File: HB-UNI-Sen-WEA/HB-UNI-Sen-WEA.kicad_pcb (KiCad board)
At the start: 2 copper layers, 66 x 55.9 mm, 21 parts, among them J1 RAIN, J10 BATT, J2 PROG, J3 WIND_DIR, J4 I2C_1, J5 LIGHTNING, J6 ANEM, J7 RAIN_Q, J8 I2C_2, J9 I2C_3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

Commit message: add mounting holes
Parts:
- added REF**: MountingHole_2.2mm_M2_Pad_Via, MountingHole:MountingHole_2.2mm_M2_Pad_Via, F.Cu at (166.4, 105.4)
- added REF**: MountingHole_2.2mm_M2_Pad_Via, MountingHole:MountingHole_2.2mm_M2_Pad_Via, F.Cu at (182.9, 68.6)
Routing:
- net GND: vias 259 -> 0
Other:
- outline, holes or cut-outs redrawn

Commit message: fix typos
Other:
- board text added: "HB-UNI-SEN-WEA-PCB"
- board text removed: "HB-UNI-SENS-WEA-PCB"
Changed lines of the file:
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@@
     (effects (font (size 1 1) (thickness 0.2)) (justify left mirror))
   )
-  (gr_text HB-UNI-SENS-WEA-PCB (at 151.13 93.98) (layer B.SilkS)
+  (gr_text HB-UNI-SEN-WEA-PCB (at 151.13 93.98) (layer B.SilkS)
     (effects (font (size 1.25 1.25) (thickness 0.3)) (justify left mirror))
   )

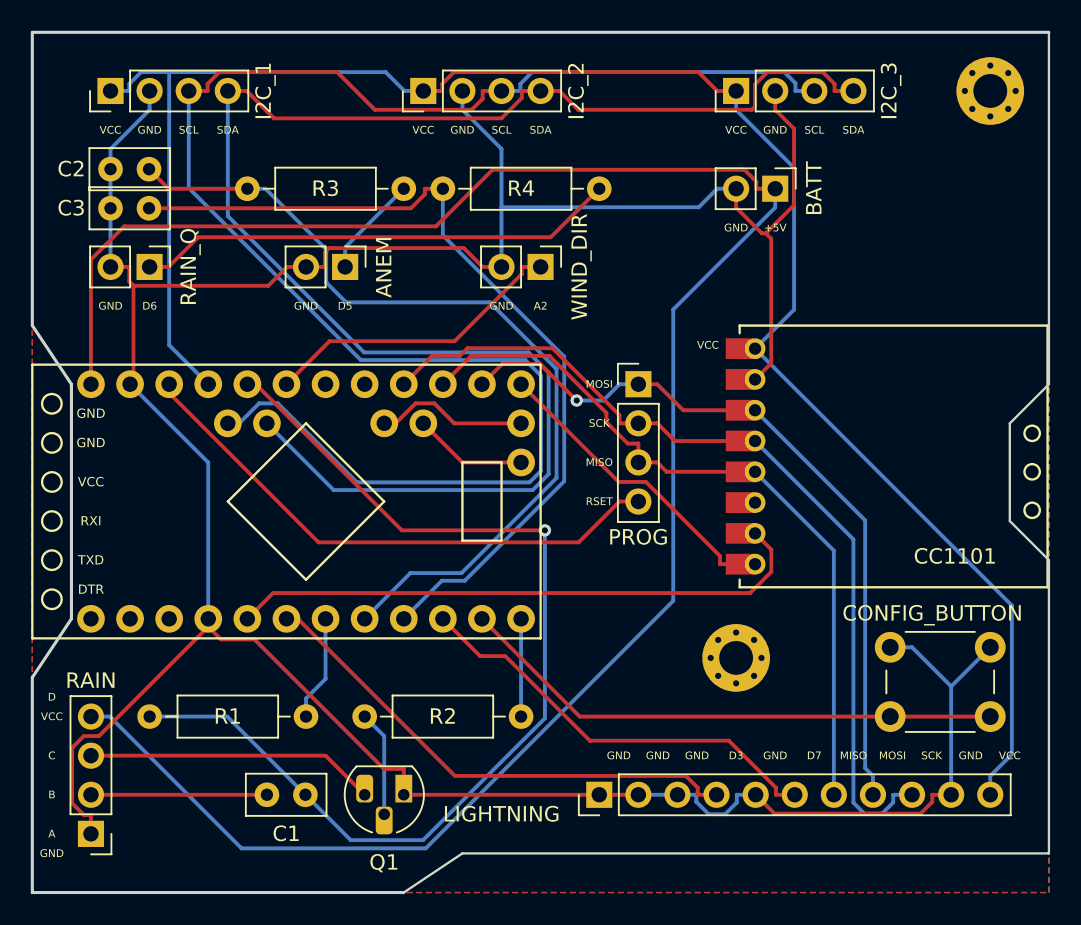
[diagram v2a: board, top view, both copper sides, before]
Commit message: updated PCB layout
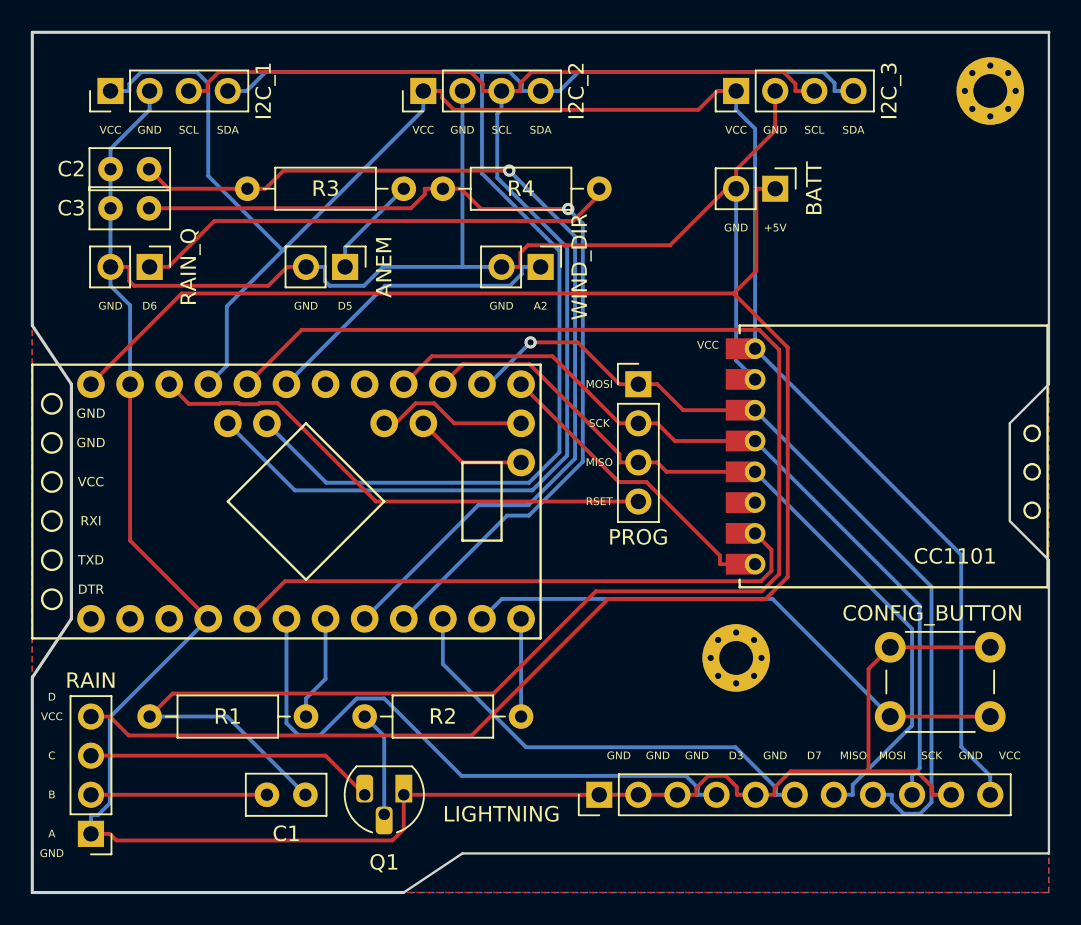
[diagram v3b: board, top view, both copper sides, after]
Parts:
- renumbered REF** to MH1, REF** to MH2
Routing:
- net /A3: track 67.8 -> 108.1 mm, vias 1 -> 0
- net /SDA: track 105.8 -> 91.5 mm
- net /SCL: track 108.6 -> 94.3 mm
- net +5V: track 133.3 -> 122.7 mm
- net /MOSI: track 48.6 -> 55.8 mm
- net /D5: track 56.4 -> 62.9 mm, vias 0 -> 1
- net /D3: track 32.9 -> 38.9 mm
- net /D6: track 56.2 -> 61.2 mm, vias 0 -> 1
- net /SCK: track 57.7 -> 53.5 mm
- net /MISO: track 48.3 -> 52.1 mm
- net /RSET: track 36.2 -> 33.8 mm
- net GND: track 209.8 -> 211.9 mm
- net /D7: track 27.9 -> 29.6 mm
- net /VCC: track 121.4 -> 120.3 mm
- net /D8: track 35.7 -> 36.7 mm
